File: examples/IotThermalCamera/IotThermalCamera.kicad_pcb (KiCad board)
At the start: 2 copper layers, 40 x 37 mm, 53 parts

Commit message: thermal camera PCB routing
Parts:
- moved jlc_th.th2 132.7 mm to (177.0, 101.5)
- moved tp_3v3 132.7 mm to (186.0, 100.0)
- moved tp_pwr 132.7 mm to (186.0, 94.0)
- moved reg_3v3.boot_cap 130.4 mm to (130.0, 97.0), turned to 90 degrees
- moved reg_3v3.fb.top_res 129.4 mm to (134.0, 97.0), turned to -90 degrees
- moved reg_3v3.hf_in_cap 128.7 mm to (134.0, 102.0), turned to 90 degrees
- moved ledr.package 128.7 mm to (180.0, 118.0)
- moved ledr.res 128.7 mm to (180.0, 116.5)
- moved reg_3v3.power_path.inductor 128.5 mm to (131.0, 107.0), turned to 180 degrees
- moved reg_3v3.en_res 127.8 mm to (132.0, 97.0), turned to -90 degrees
- moved reg_3v3.fb.bottom_res 126.7 mm to (136.0, 97.0), turned to 90 degrees
- moved reg_3v3.power_path.out_cap 124.8 mm to (128.0, 102.0), turned to 90 degrees
- moved mcu.prog 122.7 mm to (169.0, 114.7)
- moved tp_gnd 118.2 mm to (180.0, 113.0)
- moved reg_3v3.power_path.in_cap 117.8 mm to (136.0, 102.0), turned to 90 degrees
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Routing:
- net Treg_3v3.boot_cap.neg: track 0.00 -> 16.6 mm, vias 0 -> 2
- net Tv3v3: track 14.6 -> 30.1 mm, vias 0 -> 1
- net Tgnd: track 0.00 -> 14.0 mm, vias 1 -> 5
- net Tv3v0: track 0.00 -> 12.0 mm, vias 0 -> 1
- net Tpwr: track 0.00 -> 10.3 mm, vias 0 -> 3
- net Tv1v2: track 0.00 -> 10.2 mm, vias 0 -> 1
- net Tmcu.program_en_node: track 8.25 -> 0.00 mm
- net Treg_3v3.fb.output: track 0.00 -> 6.47 mm
- net Tv2v8: track 0.00 -> 5.83 mm, vias 0 -> 3
- net Treg_3v3.en_res.b: track 0.00 -> 3.45 mm
- net Treg_3v3.boot_cap.pos: track 0.00 -> 3.04 mm
- added copper zone on F.Cu, net Treg_3v3.boot_cap.neg
- added copper zone on F.Cu, net Tv3v3
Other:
- board size 40 x 37 mm -> 48 x 37 mm
- copper layers 2 -> 4

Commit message: Update IotThermalCamera.kicad_pcb
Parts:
- moved mcu.prog 49.1 mm to (120.0, 111.0)
- moved prot_3v3 45.4 mm to (172.0, 108.0), turned to 90 degrees
- moved reg_1v2.in_cap 44.9 mm to (128.0, 98.0), turned to -90 degrees
- moved reg_3v0.in_cap 44.6 mm to (128.0, 106.0), turned to -90 degrees
- moved reg_2v8.in_cap 44.0 mm to (128.0, 102.0), turned to -90 degrees
- moved reg_3v3.power_path.out_cap 44.0 mm to (172.0, 103.0), turned to -90 degrees
- moved reg_3v3.boot_cap 41.5 mm to (170.0, 108.0), turned to -90 degrees
- moved usb.conn 40.4 mm to (170.2, 115.0), turned to 90 degrees
- moved reg_1v2.ic 39.1 mm to (131.0, 98.0), turned to 0 degrees
- moved reg_3v3.power_path.inductor 39.1 mm to (169.0, 98.0), turned to 0 degrees
- moved reg_3v0.ic 38.6 mm to (131.0, 106.0), turned to 0 degrees
- moved reg_2v8.ic 38.0 mm to (131.0, 102.0), turned to 0 degrees
- moved reg_3v3.ic 38.0 mm to (169.0, 103.0), turned to -90 degrees
- moved reg_3v3.en_res 37.6 mm to (168.0, 108.0), turned to 90 degrees
- moved reg_3v3.fb.top_res 33.8 mm to (166.0, 108.0), turned to 90 degrees
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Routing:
- net Tv3v3: track 30.1 -> 18.5 mm
- net Tv2v8: vias 3 -> 4
- net Tgnd: vias 5 -> 4

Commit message: wip
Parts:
- moved mcu.vcc_cap0 6.40 mm to (163.0, 97.0), turned to 0 degrees
- moved reg_3v3.power_path.inductor 1.00 mm to (170.0, 98.0)
- turned prot_3v3 to -90 degrees
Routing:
- net Tv3v3: track 18.5 -> 20.8 mm
- net Tgnd: vias 4 -> 7

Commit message: floorplan
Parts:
- added REF**: MountingHole_2.7mm_M2.5, MountingHole:MountingHole_2.7mm_M2.5, F.Cu at (130.0, 90.0)
- added REF**: MountingHole_2.7mm_M2.5, MountingHole:MountingHole_2.7mm_M2.5, F.Cu at (170.0, 124.0)
- added REF**: MountingHole_2.7mm_M2.5, MountingHole:MountingHole_2.7mm_M2.5, F.Cu at (170.0, 90.0)
- moved jlc_th.th1 58.6 mm to (129.0, 94.0)
- moved jlc_th.th2 56.3 mm to (129.0, 119.0)
- moved tp_3v3 53.2 mm to (133.0, 95.0)
- moved ledr.res 49.4 mm to (131.0, 110.0)
- moved ledr.package 45.7 mm to (135.0, 110.0)
- moved tp_pwr 31.4 mm to (161.0, 113.0)
- moved tp_gnd 19.9 mm to (161.0, 119.0)
- moved jlc_th.th3 19.8 mm to (171.0, 94.0)
- moved mcu.prog 13.6 mm to (133.0, 115.0)
- moved usb.cc_pull.cc1 7.28 mm to (156.0, 116.0), turned to -90 degrees
- moved usb.cc_pull.cc2 6.40 mm to (158.0, 116.0), turned to 90 degrees
- moved mcu.en_pull.r 5.66 mm to (163.0, 95.0)
- moved mcu.vcc_cap0 4.47 mm to (159.0, 99.0), turned to 180 degrees
- moved mcu.vcc_cap1 4.47 mm to (159.0, 97.0), turned to 180 degrees
- moved mcu.en_pull.c 4.00 mm to (163.0, 97.0)
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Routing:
- net Ti2c_chain_0.sda: track 0.00 -> 7.87 mm
- net Treg_3v3.boot_cap.neg: track 16.6 -> 9.11 mm
- net Ti2c_chain_0.scl: track 0.00 -> 7.46 mm
- net Tmcu.program_en_node: track 0.00 -> 7.21 mm, vias 0 -> 1
- net Tusb.conn.cc.cc1: track 3.73 -> 10.6 mm
- net Tcam.device.reset: track 0.00 -> 6.89 mm
- net Tv3v0: track 12.0 -> 18.9 mm
- net Tcam.dvp8.pclk: track 0.00 -> 6.68 mm
- net Tusb.conn.cc.cc2: track 3.24 -> 7.74 mm
- net Tpwr: track 10.3 -> 13.9 mm
- net Tledr.res.a: track 0.00 -> 2.39 mm
- net Tv3v3: track 20.8 -> 22.8 mm
- net Tusb_chain_0.d_N: track 6.04 -> 6.74 mm
- net Tv2v8: vias 4 -> 3
- net Tgnd: vias 7 -> 6
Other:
- board size 48 x 37 mm -> 44 x 27 mm

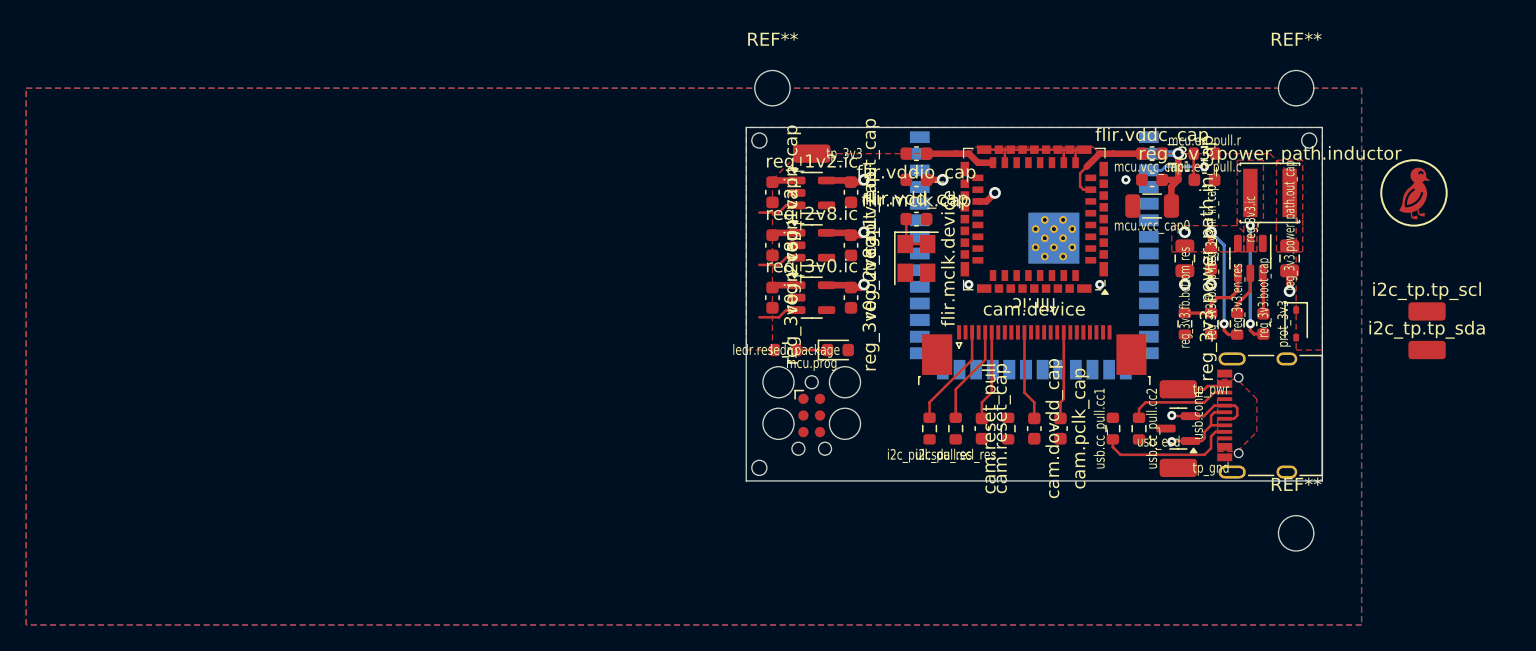
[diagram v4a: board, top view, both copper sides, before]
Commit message: lepton layout done
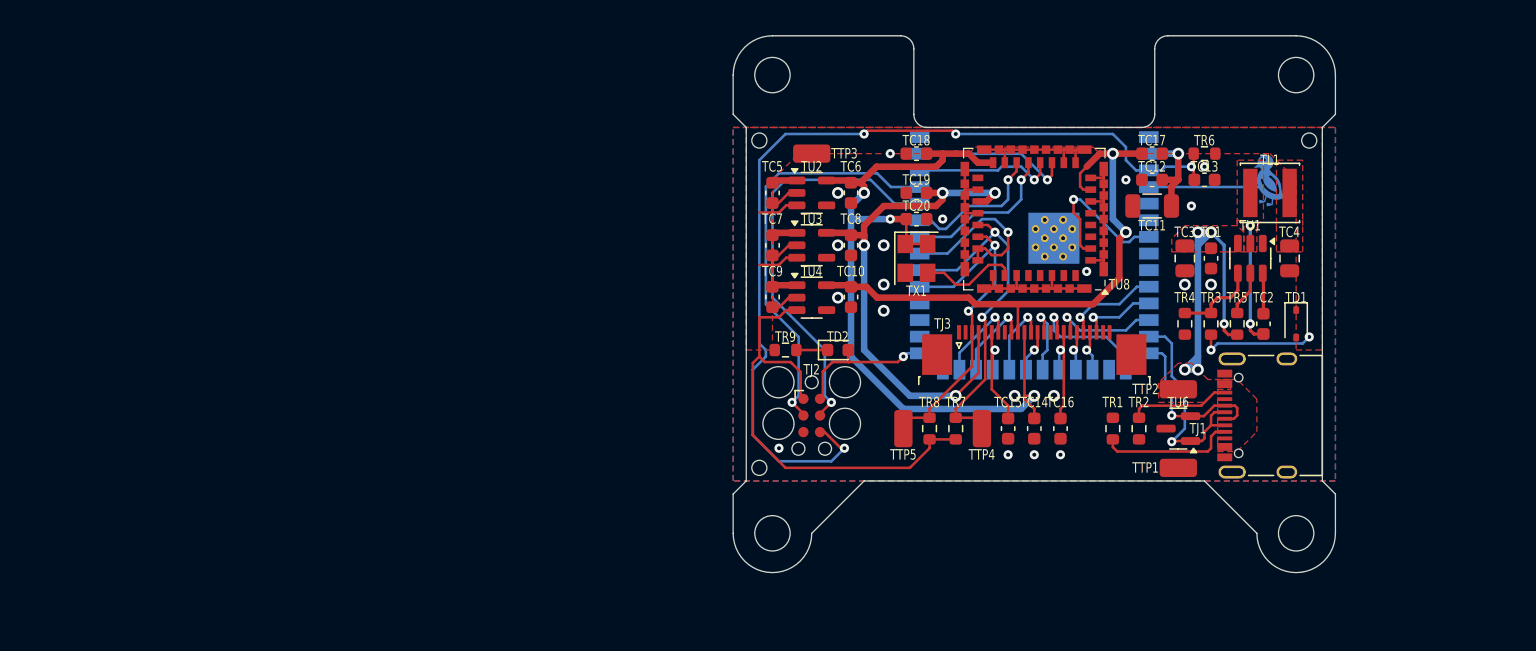
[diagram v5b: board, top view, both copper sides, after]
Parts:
- removed cam.reset_pull: ±1% 1/10W Thick Film Resistors 75V ±100ppm/? -55?~+155? 10k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, Resistor_SMD:R_0603_1608Metric
- removed svg2mod: G***, edg:Symbol_DucklingSolid
- added REF**: MountingHole_2.7mm_M2.5, MountingHole:MountingHole_2.7mm_M2.5, F.Cu at (130.0, 124.0)
- added TU7: , edg:Symbol_DucklingSolid, B.Cu at (168.0, 97.0)
- moved TTP5 40.4 mm to (140.0, 116.0), turned to 90 degrees
- moved TTP4 35.2 mm to (146.0, 116.0), turned to 90 degrees
- moved TC10 8.00 mm to (136.0, 106.0)
- moved TC5 8.00 mm to (130.0, 98.0)
- moved TC6 8.00 mm to (136.0, 98.0)
- moved TC9 8.00 mm to (130.0, 106.0)
- moved TU2 8.00 mm to (133.0, 98.0)
- moved TU4 8.00 mm to (133.0, 106.0)
- moved TC15 2.00 mm to (148.0, 116.0)
- moved REF** 1.00 mm to (130.0, 89.0)
- moved REF** 1.00 mm to (170.0, 89.0)
- moved TC19 1.00 mm to (141.0, 98.0)
- renumbered reg_3v3.hf_in_cap to TC1, reg_1v2.out_cap to TC10, mcu.vcc_cap0 to TC11, mcu.vcc_cap1 to TC12, mcu.en_pull.c to TC13, cam.dovdd_cap to TC14, cam.reset_cap to TC15, cam.pclk_cap to TC16, flir.vddc_cap to TC17, flir.vddio_cap to TC18, flir.vdd_cap to TC19, reg_3v3.boot_cap to TC2, flir.mclk.cap to TC20, reg_3v3.power_path.in_cap to TC3, reg_3v3.power_path.out_cap to TC4, reg_3v0.in_cap to TC5, reg_3v0.out_cap to TC6, reg_2v8.in_cap to TC7, reg_2v8.out_cap to TC8, reg_1v2.in_cap to TC9, prot_3v3 to TD1, ledr.package to TD2, jlc_th.th1 to TH1, jlc_th.th2 to TH2, jlc_th.th3 to TH3, usb.conn to TJ1, mcu.prog to TJ2, cam.device to TJ3, reg_3v3.power_path.inductor to TL1, usb.cc_pull.cc1 to TR1, usb.cc_pull.cc2 to TR2, reg_3v3.fb.top_res to TR3, reg_3v3.fb.bottom_res to TR4, reg_3v3.en_res to TR5, mcu.en_pull.r to TR6, i2c_pull.scl_res to TR7, i2c_pull.sda_res to TR8, ledr.res to TR9, tp_gnd to TTP1, tp_pwr to TTP2, tp_3v3 to TTP3, i2c_tp.tp_scl to TTP4, i2c_tp.tp_sda to TTP5, reg_3v3.ic to TU1, reg_3v0.ic to TU2, reg_2v8.ic to TU3, reg_1v2.ic to TU4, mcu.ic to TU5, usb_esd to TU6, flir.ic to TU8, flir.mclk.device to TX1
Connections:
- TC15 pad 1: Tcam.device.reset -> Tcam.reset
- TD2 pad 2: Tledr.signal -> Tmcu.program_boot_node
- TJ3 pad 6: Tcam.device.reset -> Tcam.reset
- TU5 pad 10: Tcam.dvp8.y4 -> Tcam.dvp8.y3
- TU5 pad 11: Tcam.dvp8.y5 -> Tcam.dvp8.y2
- TU5 pad 12: Tflir.cs -> Tcam.dvp8.y4
- TU5 pad 15: Tflir.spi.miso -> Tcam.dvp8.y5
- TU5 pad 17: Tcam.dvp8.xclk -> Tcam.dvp8.y1
- TU5 pad 18: Tcam.dvp8.pclk -> Tcam.dvp8.y0
- TU5 pad 19: Tcam.dvp8.href -> Tcam.dvp8.pclk
- TU5 pad 20: Tcam.dvp8.vsync -> Tcam.dvp8.y6
- TU5 pad 21: Tcam.dvp8.y0 -> Tcam.dvp8.xclk
- TU5 pad 22: Tcam.dvp8.y1 -> Tcam.dvp8.y7
- TU5 pad 23: Tcam.dvp8.y6 -> Tcam.reset
- TU5 pad 24: (no net) -> Tcam.dvp8.href
- TU5 pad 25: Tcam.dvp8.y7 -> Tcam.dvp8.vsync
- TU5 pad 31: (no net) -> Ti2c_chain_0.sda
- TU5 pad 32: (no net) -> Ti2c_chain_0.scl
- TU5 pad 33: (no net) -> Tflir.reset
- TU5 pad 34: (no net) -> Tflir.spi.sck
- TU5 pad 35: (no net) -> Tflir.cs
- TU5 pad 38: Tflir.spi.mosi -> Tflir.spi.miso
- TU5 pad 39: Tflir.spi.sck -> Tflir.spi.mosi
- TU5 pad 4: Ti2c_chain_0.scl -> Ttouch_duck.pad
- TU5 pad 5: Ti2c_chain_0.sda -> (no net)
- TU5 pad 6: Tledr.signal -> (no net)
- TU5 pad 7: Tflir.reset -> Tflir.vsync
- TU5 pad 8: Tcam.dvp8.y2 -> (no net)
- TU5 pad 9: Tcam.dvp8.y3 -> (no net)
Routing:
- net Tmcu.program_en_node: track 7.21 -> 70.3 mm, vias 1 -> 4
- net Tv3v0: track 18.9 -> 60.9 mm, vias 1 -> 3
- net Tv3v3: track 22.8 -> 64.7 mm, vias 1 -> 3
- net Tv2v8: track 5.83 -> 41.1 mm, vias 3 -> 4
- net Tgnd: track 14.0 -> 48.2 mm, vias 6 -> 20
- net Tv1v2: track 10.2 -> 43.3 mm, vias 1 -> 2
- net Tmcu.program_uart_node.a_tx: track 0.00 -> 31.7 mm, vias 0 -> 1
- net Tmcu.program_uart_node.b_tx: track 0.00 -> 31.6 mm, vias 0 -> 1
- net Ti2c_chain_0.scl: track 7.46 -> 27.0 mm, vias 0 -> 2
- net Ti2c_chain_0.sda: track 7.87 -> 26.2 mm, vias 0 -> 2
- net Tflir.reset: track 0.00 -> 13.1 mm, vias 0 -> 1
- net Tflir.spi.mosi: track 0.00 -> 12.0 mm, vias 0 -> 1
- net Tflir.spi.sck: track 0.00 -> 12.0 mm, vias 0 -> 1
- net Tflir.vsync: track 0.00 -> 11.9 mm, vias 0 -> 1
- net Tmcu.program_boot_node: track 0.00 -> 11.1 mm, vias 0 -> 1
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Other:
- board size 44 x 27 mm -> 46 x 41 mm
- board text added: "FLIR Lepton / RGB Camera Board v1 Sep '24"

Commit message: jlcparts for desk controller and ir cam
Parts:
- TC1, TC12, TC14, TC15, TC17, TC18, TC19, TC2, TC20: value 50V 100nF X7R ±10% 0603 Multilayer Ceramic Capacitors MLCC - SMD/SMT ROHS -> 50V 100nF X7R ±10% 0603 Multilayer Ceramic Capacitors MLCC - SMD/SMT ROHS
- TC10, TC13, TC5, TC6, TC7, TC8, TC9: value 50V 1uF X5R ±10% 0603 Multilayer Ceramic Capacitors MLCC - SMD/SMT ROHS -> 50V 1uF X5R ±10% 0603 Multilayer Ceramic Capacitors MLCC - SMD/SMT ROHS
- TC11: value 10V 22uF X5R ±10% 1206 Multilayer Ceramic Capacitors MLCC - SMD/SMT ROHS -> 25V 22uF X5R ±10% 1206 Multilayer Ceramic Capacitors MLCC - SMD/SMT ROHS
- TC16: value 50V 15pF C0G ±5% 0603 Multilayer Ceramic Capacitors MLCC - SMD/SMT ROHS -> 50V 15pF C0G ±5% 0603 Multilayer Ceramic Capacitors MLCC - SMD/SMT ROHS
- TC3, TC4: value X5R 25V ±10% 10uF 0805 Multilayer Ceramic Capacitors MLCC - SMD/SMT ROHS -> 25V 10uF X5R ±10% 0805 Multilayer Ceramic Capacitors MLCC - SMD/SMT ROHS
- TD1: value 5?A@1V 90? Single 3.53V~3.67V 200mW 3.6V SOD-323 Zener Diodes ROHS -> 3.6V~3.8V 200mW 3.6V SOD-323 Zener Diodes ROHS
- TD2: value Red 615~630nm 1.9~2.2V 0603 Light Emitting Diodes (LED) RoHS -> 5mA -40?~+85? Red 120° 0603 LED Indication - Discrete ROHS
- TL1: value 1.5A 10uH ±20% 130m? SMD Power Inductors ROHS -> 1.2A 10uH ±20% 1.6A 305m? 1210 Inductors (SMD) ROHS; footprint Inductor_SMD:L_Sunlord_SWPA4030S -> Inductor_SMD:L_1210_3225Metric
- TR1, TR2: value ±1% 1/10W Thick Film Resistors 75V ±100ppm/? -55?~+155? 5.1k? 0603 Chip Resistor - Surface Mount ROHS -> 100mW Thick Film Resistors 75V ±100ppm/? ±1% 5.1k? 0603 Chip Resistor - Surface Mount ROHS
- TR3: value ±1% 1/10W Thick Film Resistors 75V ±100ppm/? -55?~+155? 6.8k? 0603 Chip Resistor - Surface Mount ROHS -> 100mW Thick Film Resistors 75V ±100ppm/? ±1% 6.8k? 0603 Chip Resistor - Surface Mount ROHS
- TR4: value ±1% 1/10W Thick Film Resistors 75V ±100ppm/? -55?~+155? 1.5k? 0603 Chip Resistor - Surface Mount ROHS -> 100mW Thick Film Resistors 75V ±100ppm/? ±1% 1.5k? 0603 Chip Resistor - Surface Mount ROHS
- TR5: value ±1% 1/10W Thick Film Resistors 75V ±100ppm/? -55?~+155? 510k? 0603 Chip Resistor - Surface Mount ROHS -> 100mW Thick Film Resistors 75V ±100ppm/? ±1% 510k? 0603 Chip Resistor - Surface Mount ROHS
- TR6: value ±1% 1/10W Thick Film Resistors 75V ±100ppm/? -55?~+155? 10k? 0603 Chip Resistor - Surface Mount ROHS -> 100mW Thick Film Resistors 75V ±100ppm/? ±1% 10k? 0603 Chip Resistor - Surface Mount ROHS
- TR7, TR8: value ±1% 1/10W Thick Film Resistors 75V ±100ppm/? -55?~+155? 4.7k? 0603 Chip Resistor - Surface Mount ROHS -> 100mW Thick Film Resistors 75V ±100ppm/? ±1% 4.7k? 0603 Chip Resistor - Surface Mount ROHS
- TR9: value ±1% 1/10W Thick Film Resistors 75V ±100ppm/? -55?~+155? 1k? 0603 Chip Resistor - Surface Mount ROHS -> 100mW Thick Film Resistors 75V ±100ppm/? ±1% 820? 0603 Chip Resistor - Surface Mount ROHS

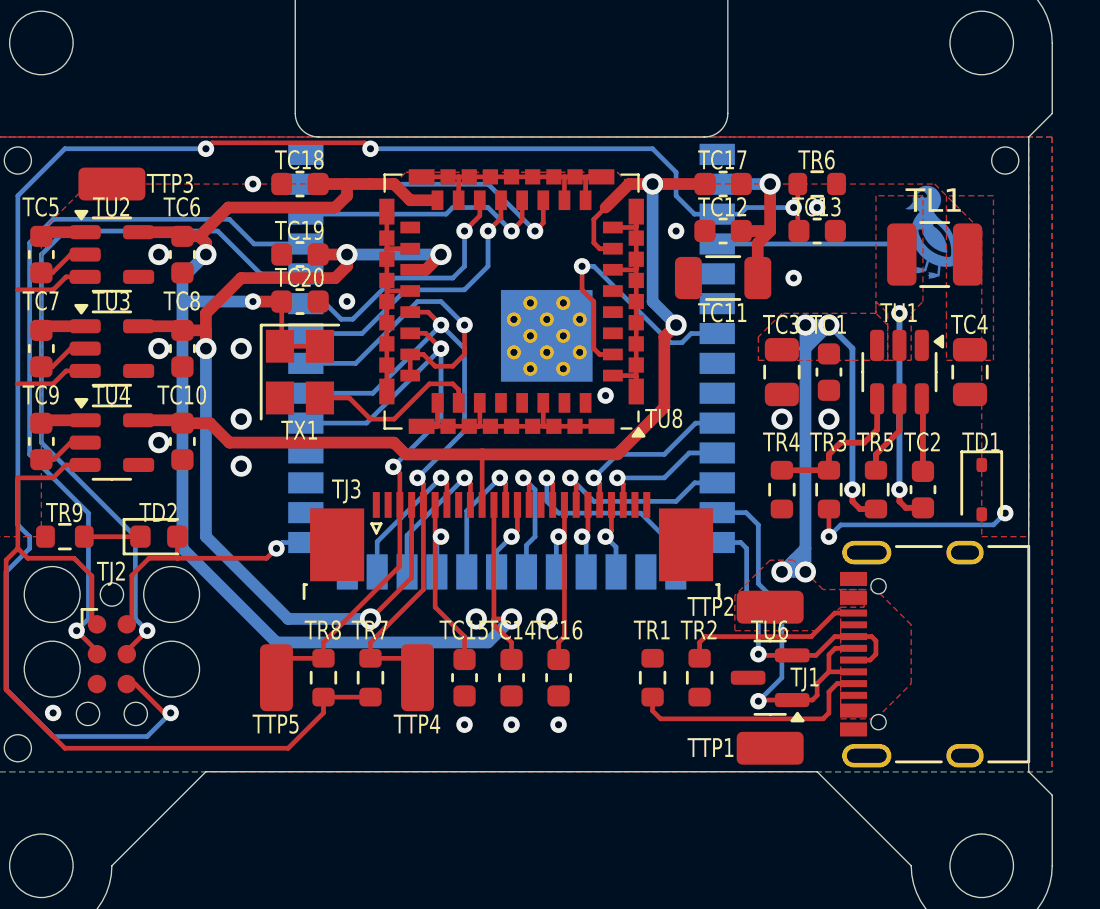
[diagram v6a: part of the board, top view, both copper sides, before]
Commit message: fab optimizations
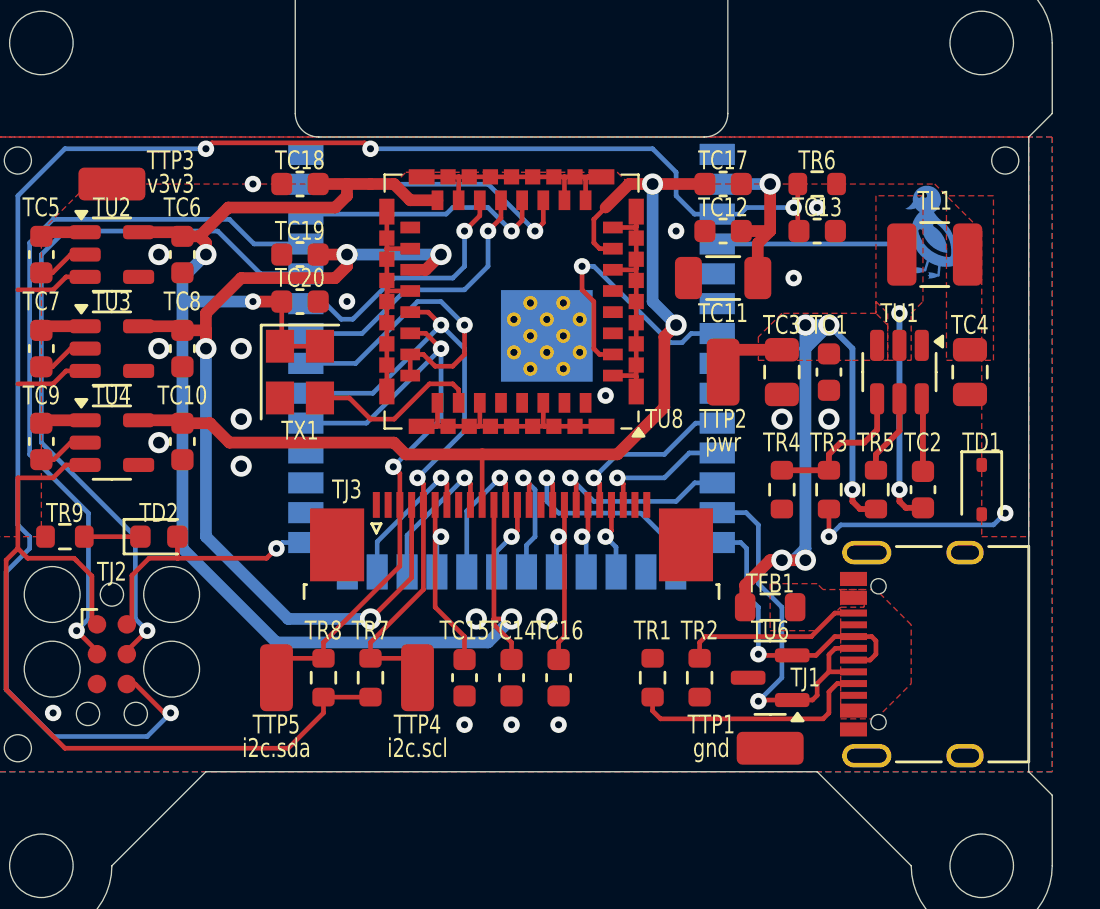
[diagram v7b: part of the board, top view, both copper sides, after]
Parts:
- added TFB1: ±25% 100?@100MHz 0805 Ferrite Beads ROHS, Inductor_SMD:L_0805_2012Metric, F.Cu at (161.0, 113.0)
- TD2: value 5mA -40?~+85? Red 120° 0603 LED Indication - Discrete ROHS -> -40?~+85? Red 0603 LED Indication - Discrete ROHS
- TTP4: value i2c_chain_0.scl -> i2c.scl
- TTP5: value i2c_chain_0.sda -> i2c.sda
- TU2: value TLV75729PDBVR -> TLV75730PDBVR
- moved TTP2 10.2 mm to (159.0, 103.0), turned to -90 degrees
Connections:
- TJ1 pad A4: Tpwr -> Tusb.pwr
- TJ1 pad A9: Tpwr -> Tusb.pwr
- TJ1 pad B4: Tpwr -> Tusb.pwr
- TJ1 pad B9: Tpwr -> Tusb.pwr
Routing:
- net Tpwr: track 24.4 -> 30.1 mm
- added copper zone on F.Cu, net Tusb.pwr
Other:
- copper layers 4 -> 2

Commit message: fix thermal camera
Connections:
- TU5 pad 33: Tflir.reset -> Tflir.shutdown
- TU5 pad 34: Tflir.spi.sck -> Tflir.reset
- TU5 pad 35: Tflir.cs -> (no net)
- TU5 pad 38: Tflir.spi.miso -> Tflir.cs
- TU5 pad 39: Tflir.spi.mosi -> Tflir.spi.sck
- TU5 pad 4: Ttouch_duck.pad -> Tflir.spi.miso
- TU5 pad 5: (no net) -> Tflir.spi.mosi
- TU5 pad 6: (no net) -> Ttouch_duck.pad
- TU8 pad 23: Tflir.reset -> Tflir.shutdown
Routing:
- net Tflir.shutdown: track 0.00 -> 13.0 mm, vias 0 -> 1
- net Tgnd: track 48.2 -> 60.1 mm, vias 20 -> 24
- net Tmcu.program_en_node: track 70.3 -> 80.5 mm, vias 4 -> 7
- net Tflir.spi.mosi: track 12.0 -> 9.08 mm
- net Tflir.cs: track 11.0 -> 8.63 mm
- net Tflir.reset: track 13.1 -> 15.4 mm
- net Tflir.spi.sck: track 12.0 -> 10.1 mm
- net Tflir.vsync: track 11.9 -> 10.8 mm
- net Ttouch_duck.pad: track 8.52 -> 9.06 mm
- net Ti2c_chain_0.sda: track 26.2 -> 26.7 mm
- net Ti2c_chain_0.scl: track 27.0 -> 27.5 mm
- net Tv1v2: track 43.3 -> 43.7 mm, vias 2 -> 0
- net Tv3v3: vias 3 -> 1
